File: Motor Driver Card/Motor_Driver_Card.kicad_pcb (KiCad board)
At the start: 2 copper layers, 129.5 x 76.2 mm, 37 parts, among them M1 MD13B, M2 MD13B, M3 MD13B, M4 MD13B, Q1 2N3904, Q2 2N3904, Q3 2N3904, Q4 2N3904

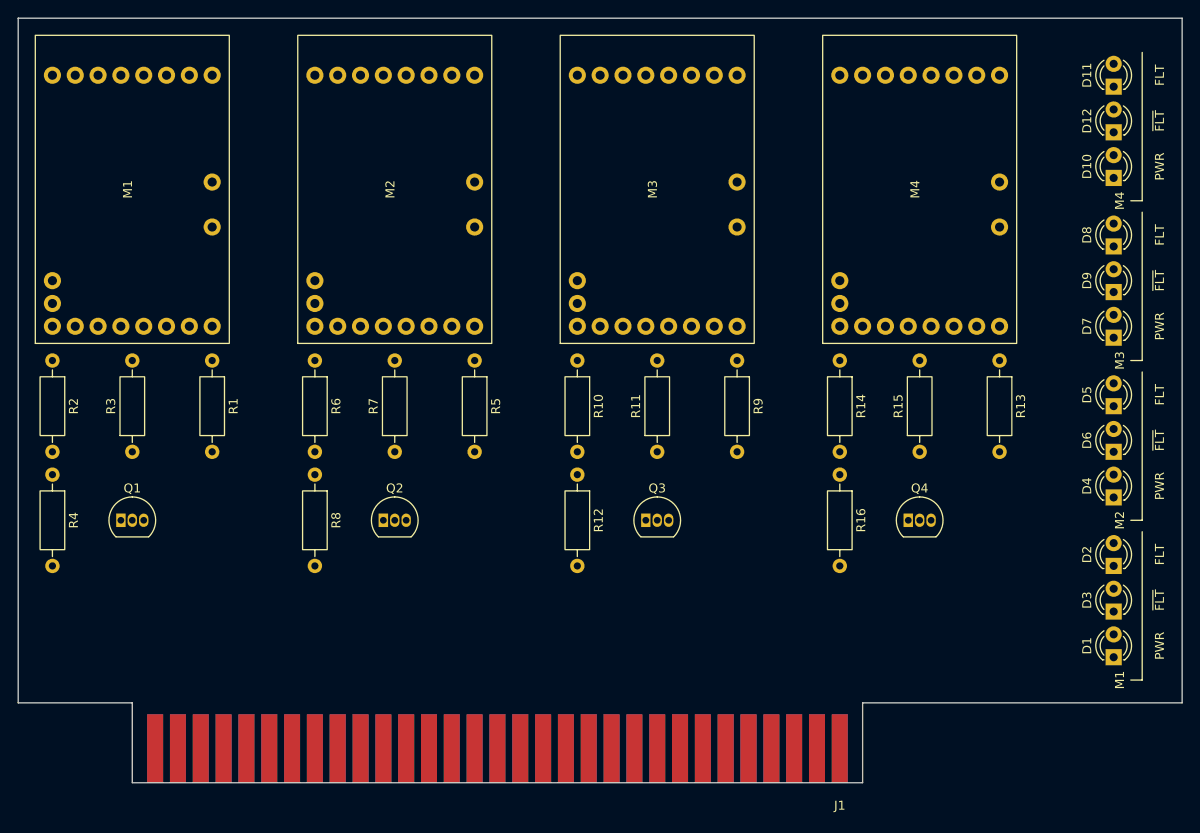
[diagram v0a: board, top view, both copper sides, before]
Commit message: Route motor driver card
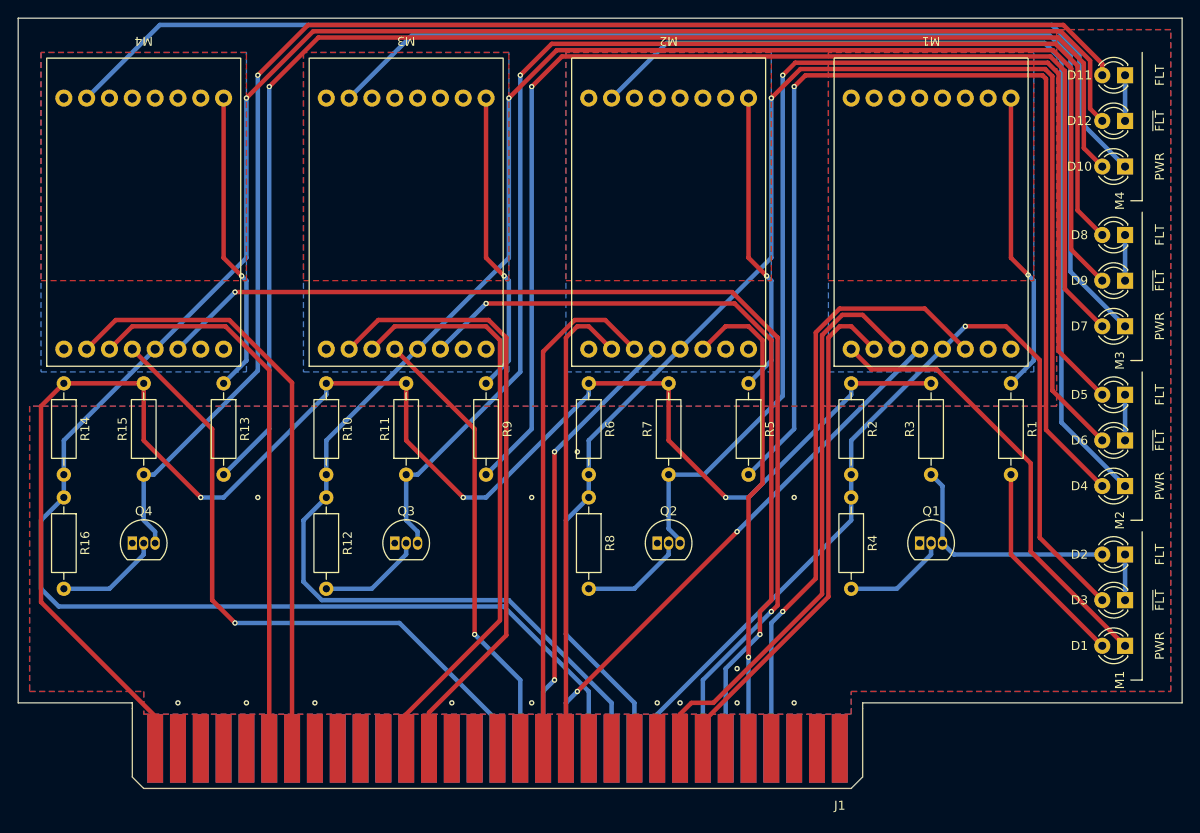
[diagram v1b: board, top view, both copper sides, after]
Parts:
- moved M1 88.9 mm to (208.3, 76.2)
- moved R3 88.9 mm to (208.3, 105.4)
- moved Q1 88.9 mm to (207.0, 113.0)
- moved R2 88.9 mm to (199.4, 95.2)
- moved R4 88.9 mm to (199.4, 108.0)
- moved R1 88.9 mm to (217.2, 95.2)
- moved Q4 86.4 mm to (119.4, 113.0)
- moved R13 86.4 mm to (129.5, 95.2)
- moved R14 86.4 mm to (111.8, 95.2)
- moved R16 86.4 mm to (111.8, 108.0)
- moved M4 86.4 mm to (120.7, 76.2)
- moved R15 86.4 mm to (120.7, 105.4)
- moved Q2 30.6 mm to (177.8, 113.0)
- moved R5 30.6 mm to (188.0, 95.2)
- moved R6 30.6 mm to (170.2, 95.2)
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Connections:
- D12 pad 2: Net-(D12-A) -> /FLT4
- D3 pad 2: Net-(D3-A) -> /FLT1
- D6 pad 2: Net-(D6-A) -> /FLT2
- D9 pad 2: Net-(D9-A) -> /FLT3
- J1 pad 12: unconnected-(J1-Pad12) -> GND
- J1 pad 13: unconnected-(J1-Pad13) -> /DIR2
- J1 pad 14: unconnected-(J1-Pad14) -> /PWM2
- J1 pad 15: unconnected-(J1-Pad15) -> GND
- J1 pad 18: unconnected-(J1-Pad18) -> GND
- J1 pad 19: unconnected-(J1-Pad19) -> /DIR3
- J1 pad 20: unconnected-(J1-Pad20) -> /PWM3
- J1 pad 21: unconnected-(J1-Pad21) -> GND
- J1 pad 24: unconnected-(J1-Pad24) -> GND
- J1 pad 25: unconnected-(J1-Pad25) -> /DIR4
- J1 pad 26: unconnected-(J1-Pad26) -> /PWM4
- J1 pad 27: unconnected-(J1-Pad27) -> GND
- J1 pad 3: unconnected-(J1-Pad3) -> GND
- J1 pad 30: unconnected-(J1-Pad30) -> GND
- J1 pad 31: unconnected-(J1-Pad31) -> +5V
- J1 pad 34: unconnected-(J1-Pad34) -> GND
- J1 pad 35: unconnected-(J1-Pad35) -> /CS1
- J1 pad 36: unconnected-(J1-Pad36) -> /CS2
- J1 pad 37: unconnected-(J1-Pad37) -> /CS3
- J1 pad 38: unconnected-(J1-Pad38) -> /CS4
- J1 pad 39: unconnected-(J1-Pad39) -> GND
- J1 pad 40: unconnected-(J1-Pad40) -> /FLT1
- J1 pad 41: unconnected-(J1-Pad41) -> /FLT2
- J1 pad 42: unconnected-(J1-Pad42) -> /FLT3
- J1 pad 43: unconnected-(J1-Pad43) -> /FLT4
- J1 pad 44: unconnected-(J1-Pad44) -> /SLP1
- J1 pad 45: unconnected-(J1-Pad45) -> /SLP2
- J1 pad 46: unconnected-(J1-Pad46) -> /SLP3
- J1 pad 47: unconnected-(J1-Pad47) -> /SLP4
- J1 pad 6: unconnected-(J1-Pad6) -> GND
- J1 pad 7: unconnected-(J1-Pad7) -> /DIR1
- J1 pad 8: unconnected-(J1-Pad8) -> /PWM1
- J1 pad 9: unconnected-(J1-Pad9) -> GND
- M1 pad 10: /Driver1/PWM -> /PWM1
- M1 pad 11: unconnected-(M1-~{SLP}-Pad11) -> /SLP1
- M1 pad 12: Net-(D3-A) -> /FLT1
- M1 pad 13: /Driver1/CS -> /CS1
- M1 pad 9: /Driver1/DIR -> /DIR1
- M2 pad 10: /Driver2/PWM -> /PWM2
- M2 pad 11: unconnected-(M2-~{SLP}-Pad11) -> /SLP2
- M2 pad 12: Net-(D6-A) -> /FLT2
- M2 pad 13: /Driver2/CS -> /CS2
- M2 pad 9: /Driver2/DIR -> /DIR2
- M3 pad 10: /Driver3/PWM -> /PWM3
- M3 pad 11: unconnected-(M3-~{SLP}-Pad11) -> /SLP3
- M3 pad 12: Net-(D9-A) -> /FLT3
- M3 pad 13: /Driver3/CS -> /CS3
- M3 pad 9: /Driver3/DIR -> /DIR3
- M4 pad 10: /Driver4/PWM -> /PWM4
- M4 pad 11: unconnected-(M4-~{SLP}-Pad11) -> /SLP4
- M4 pad 12: Net-(D12-A) -> /FLT4
- M4 pad 13: /Driver4/CS -> /CS4
- M4 pad 9: /Driver4/DIR -> /DIR4
- R10 pad 2: Net-(D9-A) -> /FLT3
- R12 pad 1: Net-(D9-A) -> /FLT3
- R14 pad 2: Net-(D12-A) -> /FLT4
- R16 pad 1: Net-(D12-A) -> /FLT4
- R2 pad 2: Net-(D3-A) -> /FLT1
- R4 pad 1: Net-(D3-A) -> /FLT1
- R6 pad 2: Net-(D6-A) -> /FLT2
- R8 pad 1: Net-(D6-A) -> /FLT2
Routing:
- net /FLT4: track 0.00 -> 241.7 mm, vias 0 -> 1
- net /FLT3: track 0.00 -> 198.9 mm, vias 0 -> 1
- net +5V: track 0.00 -> 188.4 mm, vias 0 -> 3
- net /FLT2: track 0.00 -> 160.8 mm, vias 0 -> 1
- net Net-(D11-A): track 0.00 -> 157.9 mm, vias 0 -> 1
- net Net-(D10-A): track 0.00 -> 151.7 mm, vias 0 -> 1
- net Net-(D8-A): track 0.00 -> 143.0 mm, vias 0 -> 1
- net Net-(D7-A): track 0.00 -> 136.8 mm, vias 0 -> 1
- net Net-(D10-K): track 0.00 -> 129.9 mm
- net Net-(D5-A): track 0.00 -> 129.7 mm, vias 0 -> 1
- net Net-(D4-A): track 0.00 -> 121.9 mm, vias 0 -> 1
- net /CS4: track 0.00 -> 120.6 mm, vias 0 -> 2
- net Net-(D7-K): track 0.00 -> 116.8 mm
- net Net-(D4-K): track 0.00 -> 103.8 mm
- net /FLT1: track 0.00 -> 100.6 mm, vias 0 -> 1
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- added copper zone on B.Cu, net GND
- added copper zone on F.Cu, net GND
- added copper zone on B.Cu, net Net-(D1-K)
- added copper zone on B.Cu, net Net-(D10-K)
- added copper zone on B.Cu, net Net-(D4-K)
- added copper zone on B.Cu, net Net-(D7-K)
- added copper zone on F.Cu, net Net-(M1-VIN)
- added copper zone on F.Cu, net Net-(M2-VIN)
- added copper zone on F.Cu, net Net-(M3-VIN)
- added copper zone on F.Cu, net Net-(M4-VIN)
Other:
- board size 129.5 x 76.2 mm -> 129.5 x 76.8 mm

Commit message: Apply new backplane pinouts to motor driver card
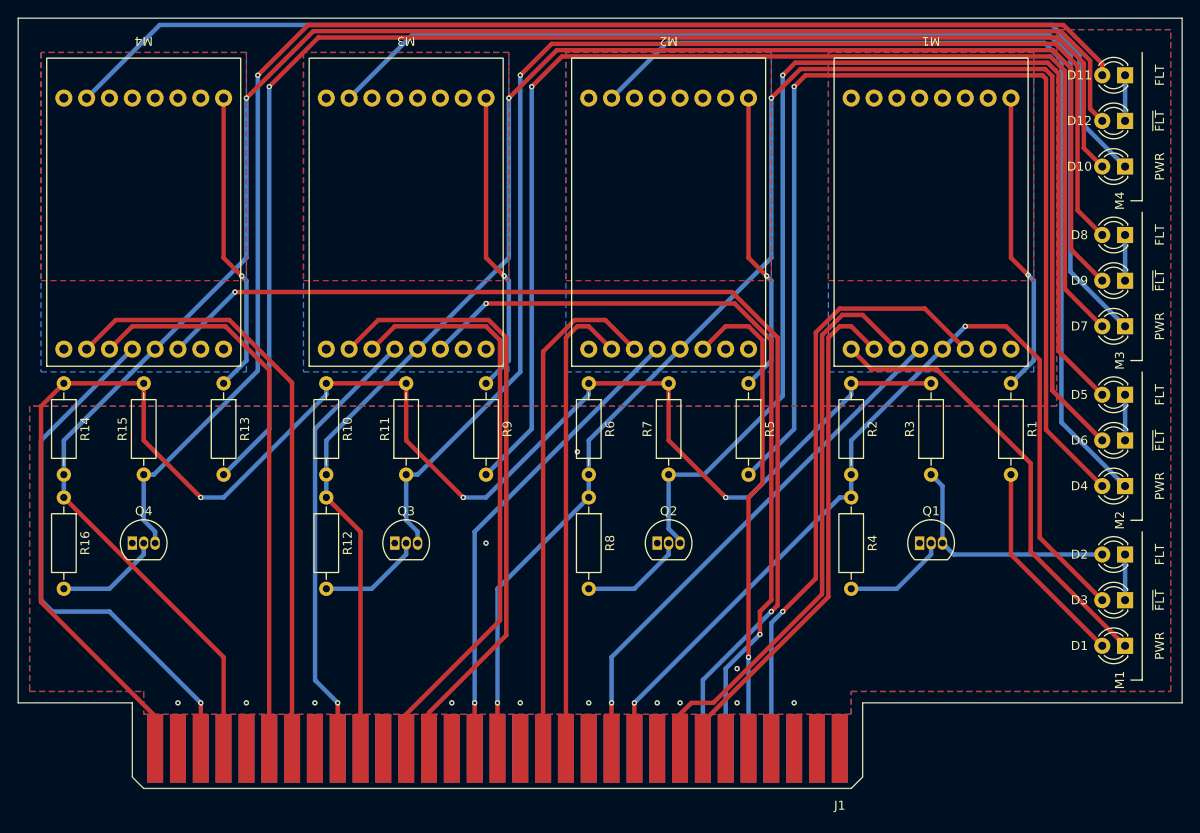
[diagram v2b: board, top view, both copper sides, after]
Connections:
- J1 pad 10: unconnected-(J1-M1_HE1-Pad10) -> /FLT1
- J1 pad 11: unconnected-(J1-M1_HE2-Pad11) -> /SLP1
- J1 pad 16: unconnected-(J1-M2_HE1-Pad16) -> /FLT2
- J1 pad 17: unconnected-(J1-M2_HE2-Pad17) -> /SLP2
- J1 pad 22: unconnected-(J1-M3_HE1-Pad22) -> /FLT3
- J1 pad 23: unconnected-(J1-ME_HE2-Pad23) -> /SLP3
- J1 pad 28: unconnected-(J1-M4_HE1-Pad28) -> /FLT4
- J1 pad 29: unconnected-(J1-M4_HE2-Pad29) -> /SLP4
- J1 pad 40: /FLT1 -> unconnected-(J1-Pad40)
- J1 pad 41: /FLT2 -> unconnected-(J1-Pad41)
- J1 pad 42: /FLT3 -> unconnected-(J1-Pad42)
- J1 pad 43: /FLT4 -> unconnected-(J1-Pad43)
- J1 pad 44: /SLP1 -> unconnected-(J1-Pad44)
- J1 pad 45: /SLP2 -> unconnected-(J1-Pad45)
- J1 pad 46: /SLP3 -> unconnected-(J1-Pad46)
- J1 pad 47: /SLP4 -> unconnected-(J1-Pad47)
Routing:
- net /FLT4: track 241.7 -> 193.8 mm
- net /FLT3: track 198.9 -> 173.1 mm
- net /SLP4: track 72.0 -> 59.7 mm
- net /SLP2: track 49.7 -> 52.9 mm, vias 2 -> 1
- net /SLP1: track 60.8 -> 58.7 mm, vias 2 -> 1
- net /FLT1: track 100.6 -> 102.4 mm, vias 1 -> 2
- net /SLP3: track 50.2 -> 49.2 mm
- net /FLT2: vias 1 -> 2
- net GND: vias 14 -> 13

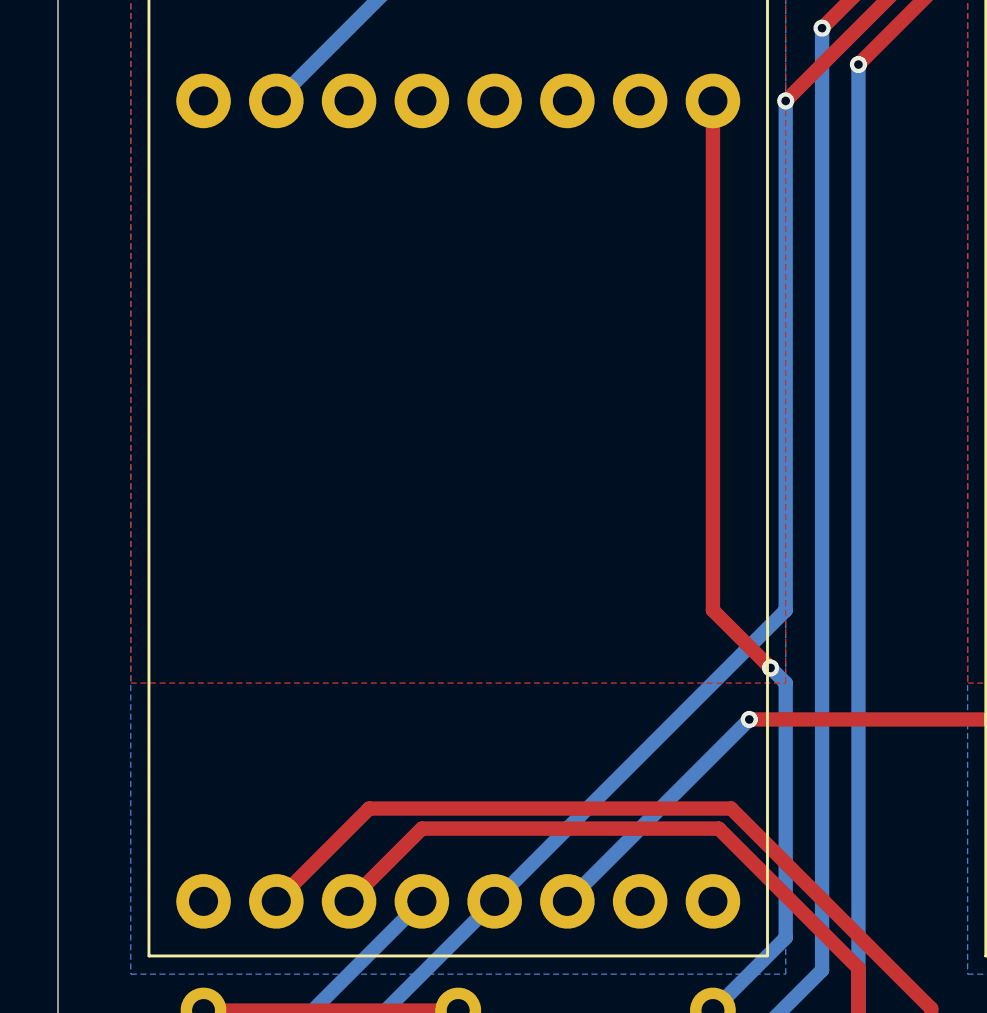
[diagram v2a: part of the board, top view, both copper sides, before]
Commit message: added silkscreen logo and labeling to motor driver card
Still needs thermistors added
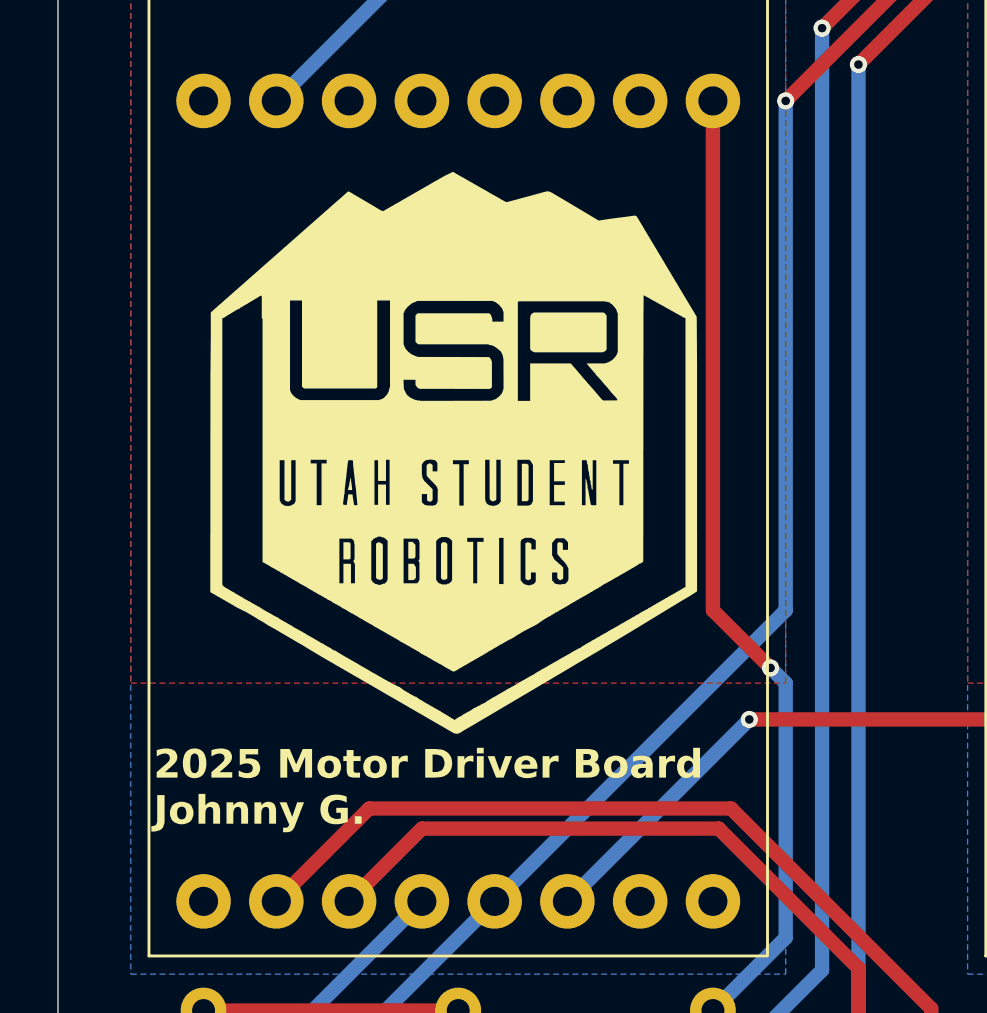
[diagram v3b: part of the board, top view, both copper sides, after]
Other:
- board text added: "2025 Motor Driver Board Johnny G."

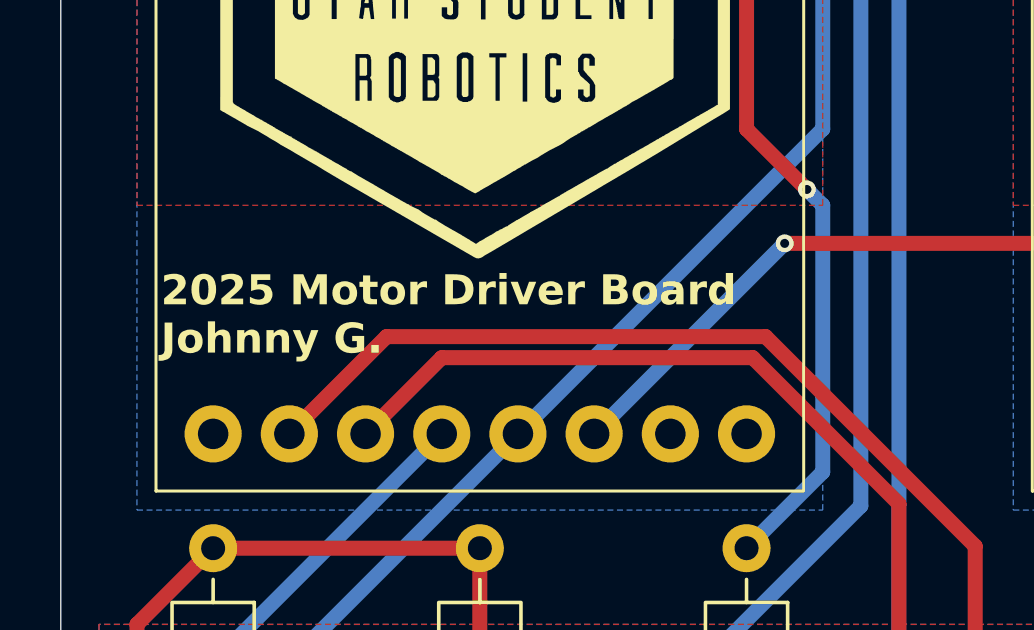
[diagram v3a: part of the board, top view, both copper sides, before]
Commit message: Modify silkscreen on motor driver card
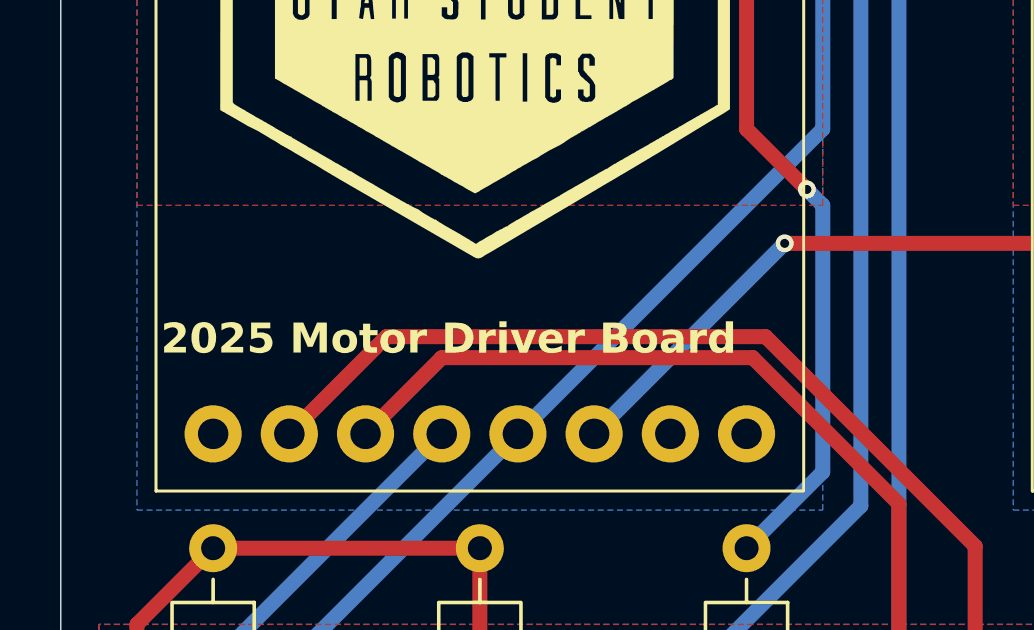
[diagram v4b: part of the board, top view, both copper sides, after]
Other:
- board text added: "2025 Motor Driver Board"
- board text removed: "2025 Motor Driver Board Johnny G."
- board text removed: "JG Motor Driver Board 25-26"
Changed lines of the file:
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@@
 		)
 	)
-	(gr_text "2025 Motor Driver Board\nJohnny G."
-		(at 110.0161 88.8522 -0)
+	(gr_text "2025 Motor Driver Board"
+		(at 110.0161 88.8522 0)
 		(layer "F.SilkS")
 		(effects
@@
 			)
 			(justify bottom)
-		)
-	)
-	(gr_text "JG\nMotor Driver Board 25-26"
-		(at 107.95 129.54 0)
-		(layer "B.SilkS")
-		(effects
-			(font
-				(size 1 1)
-				(thickness 0.1)
-			)
-			(justify right bottom mirror)
 		)
 	)
@@
 			(keep_text_aligned yes)
 		)
-		(gr_text "129.54"
+		(gr_text "5100"
 			(at 171.45 38.84 0)
 			(layer "F.Cu")
@@
 			(keep_text_aligned yes)
 		)
-		(gr_text "76.2"
+		(gr_text "3000"
 			(at 252.2 92.71 90)
 			(layer "F.Cu")
